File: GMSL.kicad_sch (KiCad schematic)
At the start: 33 parts, among them U6 MAX9295A, Y1 Resonator_25MHz_ABM8G

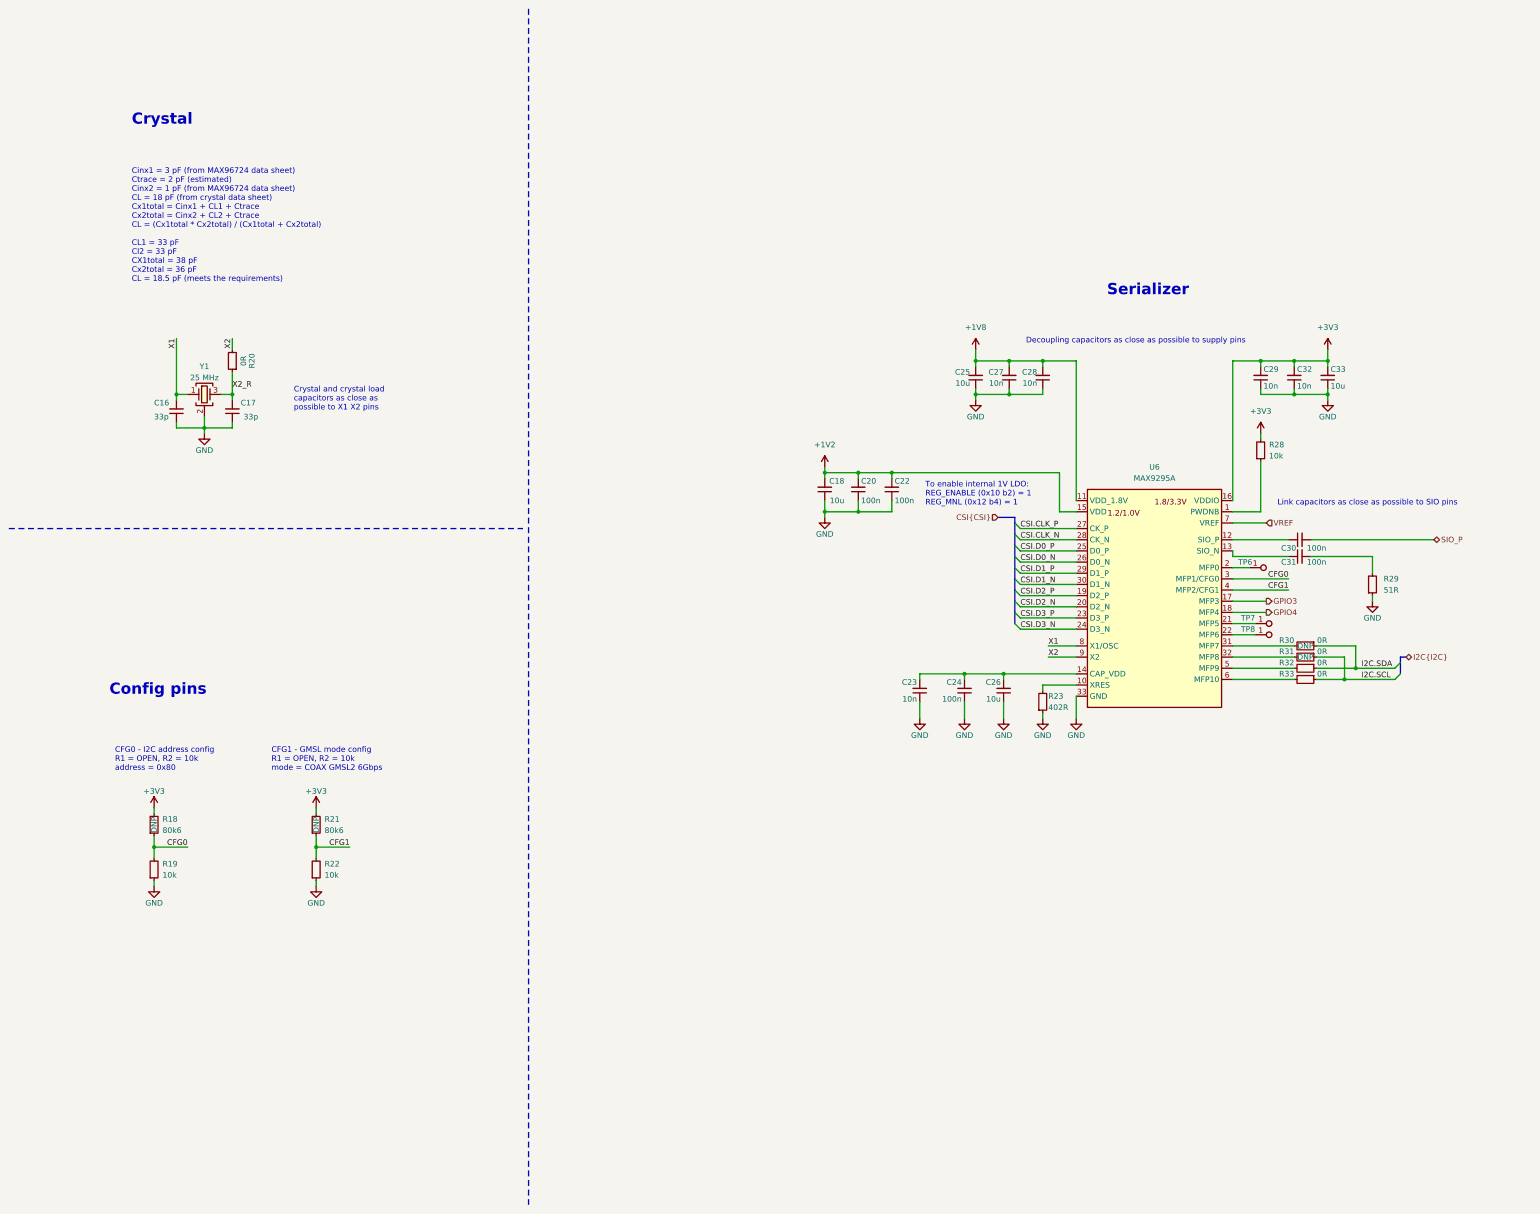
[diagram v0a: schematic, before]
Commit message: [#66847] Make schematic hierarchical
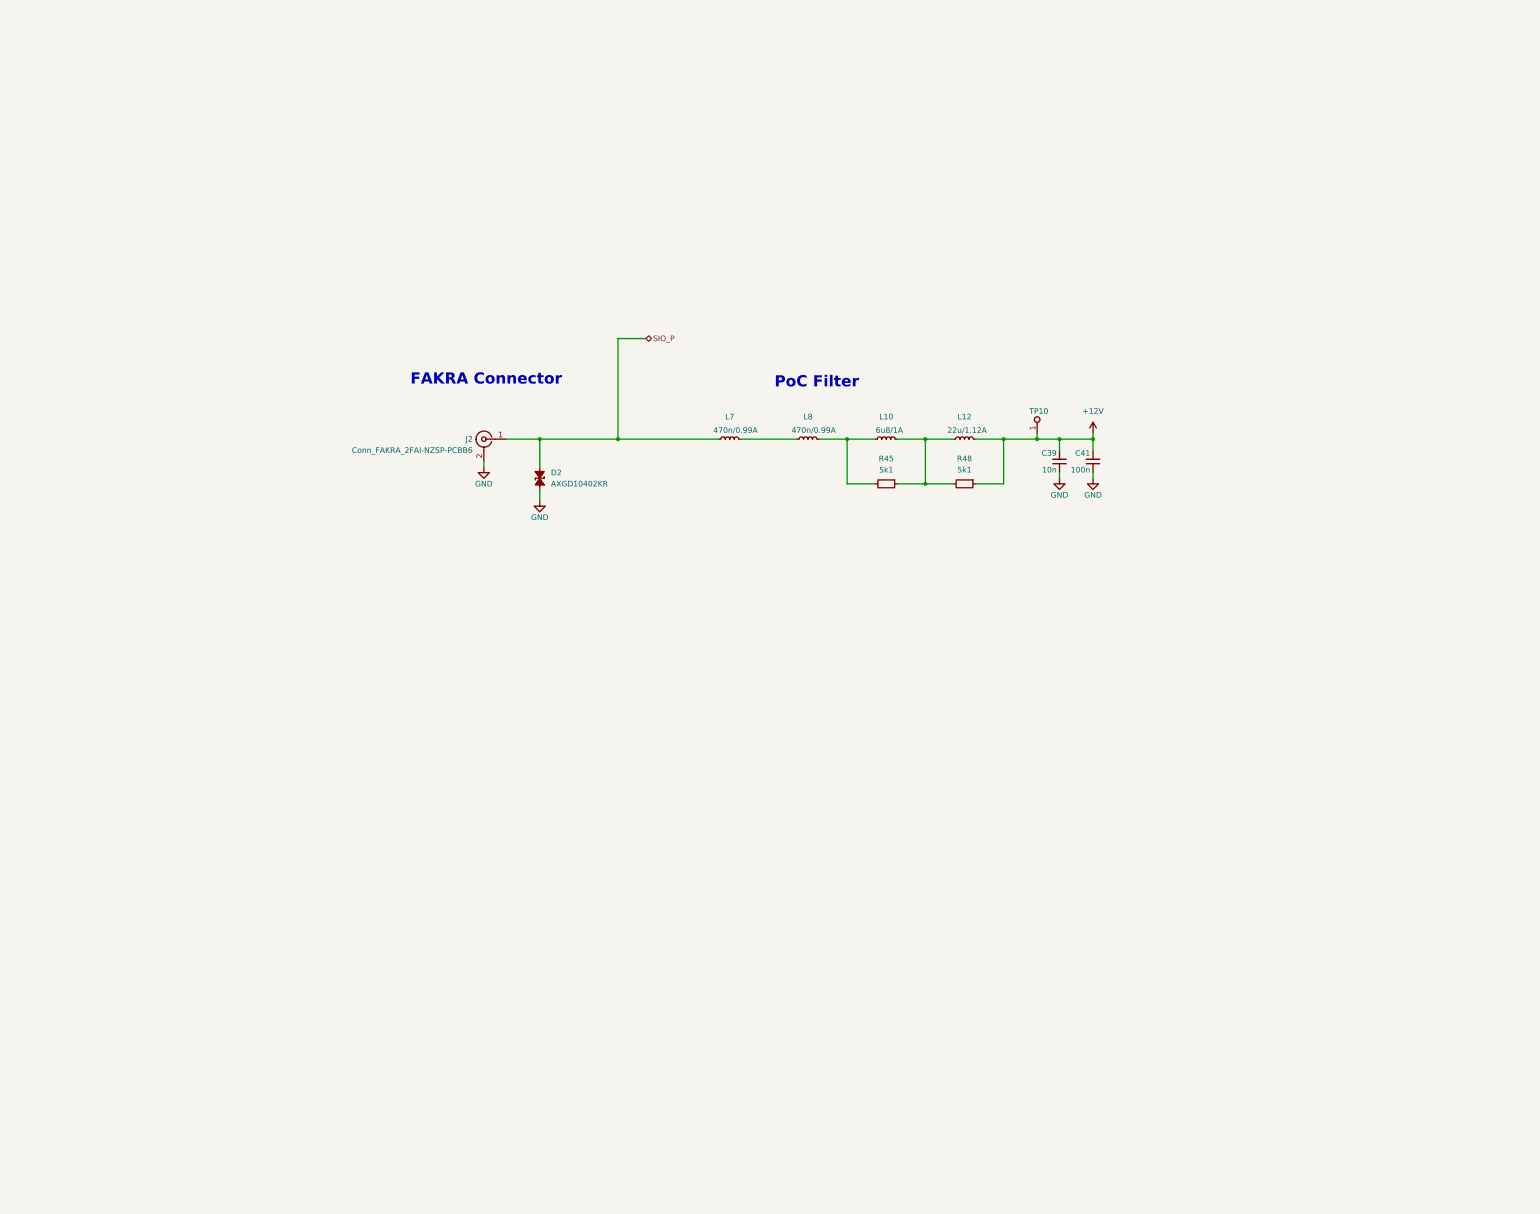
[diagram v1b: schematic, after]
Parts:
- removed C16, C17: C_33p_0402, antmicro-footprints:C_0402_1005Metric, symbol antmicroCapacitors0402:C_33p_0402
- removed C18, C25, C26, C33: C_10u_0402, antmicro-footprints:C_0402_1005Metric, symbol antmicroCapacitors0402:C_10u_0402
- removed C20, C22, C24, C30, C31: C_100n_0402, antmicro-footprints:C_0402_1005Metric, symbol antmicroCapacitors0402:C_100n_0402
- removed C23, C27, C28, C29, C32: C_10n_0402, antmicro-footprints:C_0402_1005Metric, symbol antmicroCapacitors0402:C_10n_0402
- removed R18, R21: R_80k6_0402, antmicro-footprints:R_0402_1005Metric, symbol antmicroResistors0402:R_80k6_0402
- removed R19, R22, R28: R_10k_0402, antmicro-footprints:R_0402_1005Metric, symbol antmicroResistors0402:R_10k_0402
- removed R20, R30, R31, R32, R33: R_0R_0402, antmicro-footprints:R_0402_1005Metric, symbol antmicroResistors0402:R_0R_0402
- removed R23: R_402R_0402, antmicro-footprints:R_0402_1005Metric, symbol antmicroResistors0402:R_402R_0402
- removed R29: R_51R_0402, antmicro-footprints:R_0402_1005Metric, symbol antmicroResistors0402:R_51R_0402
- removed TP6, TP7, TP8: TP_1.5mm_SMD, antmicro-footprints:TP_SMD_1.5mm, symbol antmicroTestPoints:TP_1.5mm_SMD
- removed U6: MAX9295A, antmicro-footprints:QFN-32-1EP_5x5mm, symbol antmicroInterfaceControllers:MAX9295A
- removed Y1: Resonator_25MHz_ABM8G, antmicro-footprints:Resonator_SMD_Abracon_ABM8G_3.2x2.5mm, symbol antmicroResonators:Resonator_25MHz_ABM8G
- added C39: C_10n_0402, antmicro-footprints:C_0402_1005Metric, symbol antmicroCapacitors0402:C_10n_0402
- added C41: C_100n_0402, antmicro-footprints:C_0402_1005Metric, symbol antmicroCapacitors0402:C_100n_0402
- added D2: AXGD10402KR, antmicro-footprints:D_0402_1005Metric, symbol antmicroTVSDiodes:AXGD10402KR
- added J2: Conn_FAKRA_2FAI-NZSP-PCBB6, antmicro-footprints:Conn_FAKRA_59S2AQ-40MT5-Z_1, symbol antmicroCoaxialConnectorsRF:Conn_FAKRA_59S2AQ-40MT5-Z_1
- added L10: L_6u8_1A_Coilcraft-1210POC, antmicro-footprints:L_Coilcraft-1210POC, symbol antmicroFixedInductors:L_6u8_1A_Coilcraft-1210POC
- added L12: L_22u_1.12A_Coilcraft-MSS6132T, antmicro-footprints:L_Coilcraft-MSS6132T, symbol antmicroFixedInductors:L_22u_1.12A_Coilcraft-MSS6132T
- added L7, L8: L_470n_1A_Coilcraft-PFL1609, antmicro-footprints:L_Coilcraft-PFL1609, symbol antmicroFixedInductors:L_470n_1A_Coilcraft-PFL1609
- added R45, R48: R_5k1_0402, antmicro-footprints:R_0402_1005Metric, symbol antmicroResistors0402:R_5k1_0402
- added TP10: TP_1.5mm_SMD, antmicro-footprints:TP_SMD_1.5mm, symbol antmicroTestPoints:TP_1.5mm_SMD
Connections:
- net GND: now also C39.1, C41.1, D2.2 (A), J2.2, J2.3, J2.4, J2.5
- net SIO_P: now also D2.1 (C), J2.1, L7.2
- new net: L7.1, L8.2
- new net: L10.1, L12.2, R45.1, R48.2
- new net: L10.2, L8.1, R45.2
- new net +12V: C39.2, C41.2, L12.1, R48.1, TP10.1
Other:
- note added: "FAKRA Connector"
- note added: "PoC Filter"
- note removed: "CFG0 - I2C address config R1 = OPEN, R2 = 10k address = 0x80"
- note removed: "CFG1 - GMSL mode config R1 = OPEN, R2 = 10k mode = COAX GMSL2 6Gbps"
- note removed: "Cinx1 = 3 pF (from MAX96724 data sheet) Ctrace = 2 pF (estimated) Cinx2 = 1 pF (from MAX96724 data sheet) CL = 18 pF (from crystal data sheet) Cx1total = Cinx1 + CL1 + Ctrace Cx2total = Cinx2 + CL2 + Ctrace CL = (Cx1total * Cx2total) / (Cx1total + Cx2total) CL1 = 33 pF Cl2 = 33 pF CX1total = 38 pF Cx2total = 36 pF CL = 18.5 pF (meets the requirements)"
- note removed: "Config pins"
- note removed: "Crystal"
- note removed: "Crystal and crystal load capacitors as close as possible to X1 X2 pins"
- note removed: "Decoupling capacitors as close as possible to supply pins"
- note removed: "Link capacitors as close as possible to SIO pins"
- note removed: "Serializer"
- note removed: "To enable internal 1V LDO: REG_ENABLE (0x10 b2) = 1 REG_MNL (0x12 b4) = 1"

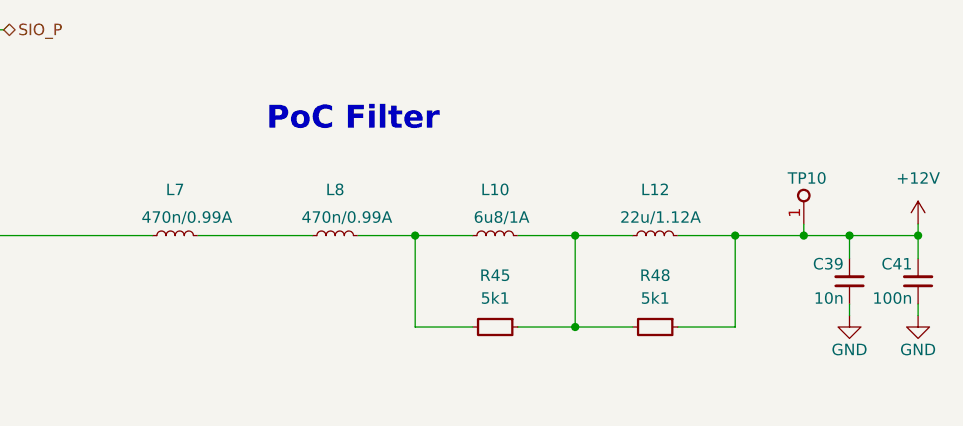
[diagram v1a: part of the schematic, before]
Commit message: [#66847] unDNP pullups on I2C; update pcb from sch
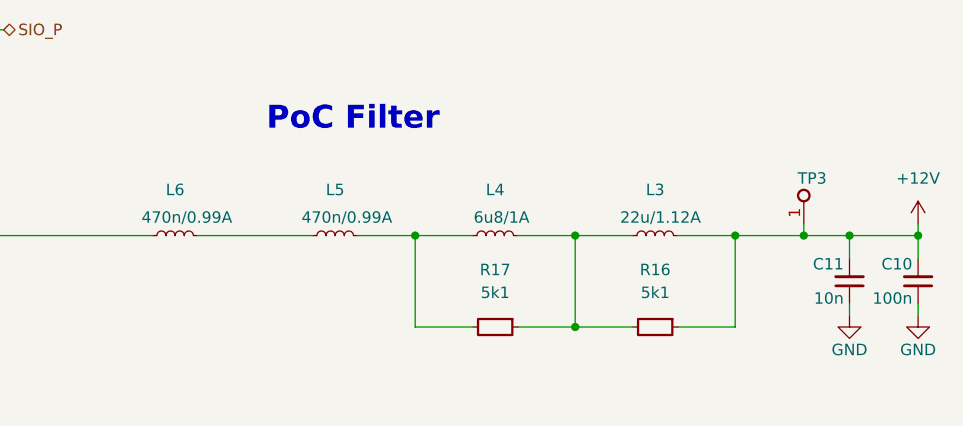
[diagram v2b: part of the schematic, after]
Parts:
- renumbered C41 to C10, C39 to C11, L12 to L3, L10 to L4, L8 to L5, L7 to L6, R48 to R16, R45 to R17, TP10 to TP3
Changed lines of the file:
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@@
   (symbol (lib_id "antmicroFixedInductors:L_470n_1A_Coilcraft-PFL1609") (at 179.07 111.76 0) (mirror y) (unit 1)
     (in_bom yes) (on_board yes) (dnp no)
-    (property "Reference" "L7" (at 176.53 106.68 0)
+    (property "Reference" "L6" (at 176.53 106.68 0)
       (effects (font (size 1.27 1.27) (thickness 0.15)))
     )
@@
       (project "gmsl-serializer"
         (path "/dbd1044a-3803-4c19-8db2-96636cba7198/48e64e6a-17fe-4036-8da5-09c7c938a7f3"
-          (reference "L7") (unit 1)
+          (reference "L6") (unit 1)
         )
       )
@@
   (symbol (lib_id "antmicroResistors0402:R_5k1_0402") (at 214.63 121.92 0) (mirror y) (unit 1)
     (in_bom yes) (on_board yes) (dnp no) (fields_autoplaced)
-    (property "Reference" "R45" (at 212.09 116.205 0)
+    (property "Reference" "R17" (at 212.09 115.57 0)
       (effects (font (size 1.27 1.27) (thickness 0.15)))
     )
@@
       (effects (font (size 1.27 1.27) (thickness 0.15)) (justify left bottom) hide)
     )
-    (property "Val" "5k1" (at 212.09 118.745 0)
+    (property "Val" "5k1" (at 212.09 118.11 0)
       (effects (font (size 1.27 1.27) (thickness 0.15)))
     )
@@
       (project "gmsl-serializer"
         (path "/dbd1044a-3803-4c19-8db2-96636cba7198/48e64e6a-17fe-4036-8da5-09c7c938a7f3"
-          (reference "R45") (unit 1)
+          (reference "R17") (unit 1)
         )
       )
@@
   (symbol (lib_id "antmicroCapacitors0402:C_10n_0402") (at 251.46 119.38 270) (mirror x) (unit 1)
     (in_bom yes) (on_board yes) (dnp no)
-    (property "Reference" "C39" (at 250.825 114.935 90)
+    (property "Reference" "C11" (at 250.825 114.935 90)
       (effects (font (size 1.27 1.27) (thickness 0.15)) (justify right))
     )
@@
       (project "gmsl-serializer"
         (path "/dbd1044a-3803-4c19-8db2-96636cba7198/48e64e6a-17fe-4036-8da5-09c7c938a7f3"
-          (reference "C39") (unit 1)
+          (reference "C11") (unit 1)
         )
       )
@@
   (symbol (lib_id "antmicroFixedInductors:L_6u8_1A_Coilcraft-1210POC") (at 214.63 111.76 0) (mirror y) (unit 1)
     (in_bom yes) (on_board yes) (dnp no)
-    (property "Reference" "L10" (at 212.09 106.68 0)
+    (property "Reference" "L4" (at 212.09 106.68 0)
       (effects (font (size 1.27 1.27) (thickness 0.15)))
     )
@@
       (project "gmsl-serializer"
         (path "/dbd1044a-3803-4c19-8db2-96636cba7198/48e64e6a-17fe-4036-8da5-09c7c938a7f3"
-          (reference "L10") (unit 1)
+          (reference "L4") (unit 1)
         )
       )
@@
   (symbol (lib_id "antmicroResistors0402:R_5k1_0402") (at 232.41 121.92 0) (mirror y) (unit 1)
     (in_bom yes) (on_board yes) (dnp no) (fields_autoplaced)
-    (property "Reference" "R48" (at 229.87 116.205 0)
+    (property "Reference" "R16" (at 229.87 115.57 0)
       (effects (font (size 1.27 1.27) (thickness 0.15)))
     )
@@
       (effects (font (size 1.27 1.27) (thickness 0.15)) (justify left bottom) hide)
     )
-    (property "Val" "5k1" (at 229.87 118.745 0)
+    (property "Val" "5k1" (at 229.87 118.11 0)
       (effects (font (size 1.27 1.27) (thickness 0.15)))
     )
@@
       (project "gmsl-serializer"
         (path "/dbd1044a-3803-4c19-8db2-96636cba7198/48e64e6a-17fe-4036-8da5-09c7c938a7f3"
-          (reference "R48") (unit 1)
+          (reference "R16") (unit 1)
         )
       )
@@
   (symbol (lib_id "antmicroFixedInductors:L_22u_1.12A_Coilcraft-MSS6132T") (at 232.41 111.76 0) (mirror y) (unit 1)
     (in_bom yes) (on_board yes) (dnp no)
-    (property "Reference" "L12" (at 229.87 106.68 0)
+    (property "Reference" "L3" (at 229.87 106.68 0)
       (effects (font (size 1.27 1.27) (thickness 0.15)))
     )
@@
       (project "gmsl-serializer"
         (path "/dbd1044a-3803-4c19-8db2-96636cba7198/48e64e6a-17fe-4036-8da5-09c7c938a7f3"
-          (reference "L12") (unit 1)
+          (reference "L3") (unit 1)
         )
       )
@@
   (symbol (lib_id "antmicroTestPoints:TP_1.5mm_SMD") (at 246.38 110.49 270) (mirror x) (unit 1)
     (in_bom yes) (on_board yes) (dnp no)
-    (property "Reference" "TP10" (at 248.92 105.41 90)
+    (property "Reference" "TP3" (at 248.92 105.41 90)
       (effects (font (size 1.27 1.27) (thickness 0.15)) (justify right))
     )
@@
       (project "gmsl-serializer"
         (path "/dbd1044a-3803-4c19-8db2-96636cba7198/48e64e6a-17fe-4036-8da5-09c7c938a7f3"
-          (reference "TP10") (unit 1)
+          (reference "TP3") (unit 1)
         )
       )
@@
   (symbol (lib_id "antmicroFixedInductors:L_470n_1A_Coilcraft-PFL1609") (at 196.85 111.76 0) (mirror y) (unit 1)
     (in_bom yes) (on_board yes) (dnp no)
-    (property "Reference" "L8" (at 194.31 106.68 0)
+    (property "Reference" "L5" (at 194.31 106.68 0)
       (effects (font (size 1.27 1.27) (thickness 0.15)))
     )
@@
       (project "gmsl-serializer"
         (path "/dbd1044a-3803-4c19-8db2-96636cba7198/48e64e6a-17fe-4036-8da5-09c7c938a7f3"
-          (reference "L8") (unit 1)
+          (reference "L5") (unit 1)
         )
       )
@@
   (symbol (lib_id "antmicroCapacitors0402:C_100n_0402") (at 259.08 119.38 270) (mirror x) (unit 1)
     (in_bom yes) (on_board yes) (dnp no)
-    (property "Reference" "C41" (at 258.445 114.935 90)
+    (property "Reference" "C10" (at 258.445 114.935 90)
       (effects (font (size 1.27 1.27) (thickness 0.15)) (justify right))
     )
@@
       (project "gmsl-serializer"
         (path "/dbd1044a-3803-4c19-8db2-96636cba7198/48e64e6a-17fe-4036-8da5-09c7c938a7f3"
-          (reference "C41") (unit 1)
-        )
-      )
+          (reference "C10") (unit 1)
+        )
+      )

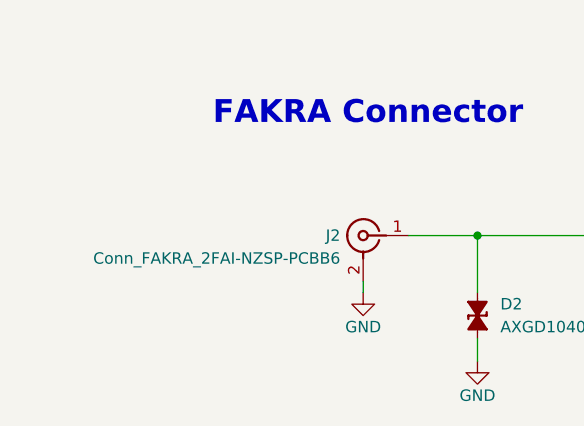
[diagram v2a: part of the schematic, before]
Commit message: [#66847] Update DNP style; Update from lib; Fix CSI bus definition
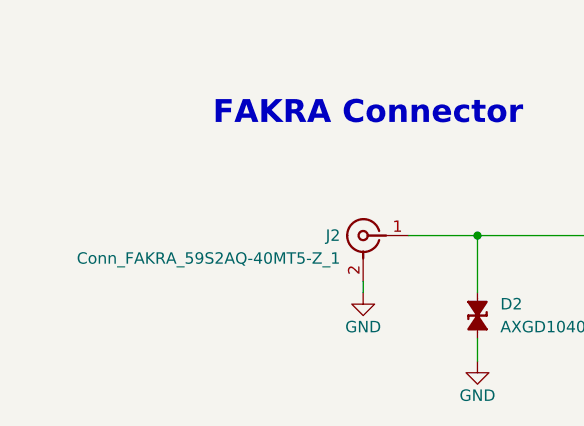
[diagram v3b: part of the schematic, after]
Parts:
- J2: value Conn_FAKRA_2FAI-NZSP-PCBB6 -> Conn_FAKRA_59S2AQ-40MT5-Z_1
- TP3: now left out of the parts list
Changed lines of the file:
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@@
       (effects (font (size 1.27 1.27) (thickness 0.15)) (justify left))
     )
-    (property "Value" "Conn_FAKRA_2FAI-NZSP-PCBB6" (at 118.11 114.3 0)
+    (property "Value" "Conn_FAKRA_59S2AQ-40MT5-Z_1" (at 118.11 114.3 0)
       (effects (font (size 1.27 1.27) (thickness 0.15)) (justify left))
     )
@@
   )
   (symbol (lib_id "antmicroTestPoints:TP_1.5mm_SMD") (at 246.38 110.49 270) (mirror x) (unit 1)
-    (in_bom yes) (on_board yes) (dnp no)
+    (in_bom no) (on_board yes) (dnp no)
     (property "Reference" "TP3" (at 248.92 105.41 90)
       (effects (font (size 1.27 1.27) (thickness 0.15)) (justify right))
